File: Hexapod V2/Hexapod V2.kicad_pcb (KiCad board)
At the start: 4 copper layers, 140 x 90 mm, 43 parts, among them J1 Battery, U1 MPU6050, U2 NRF24L01_Breakout, U3 ACS712xLCTR-05B

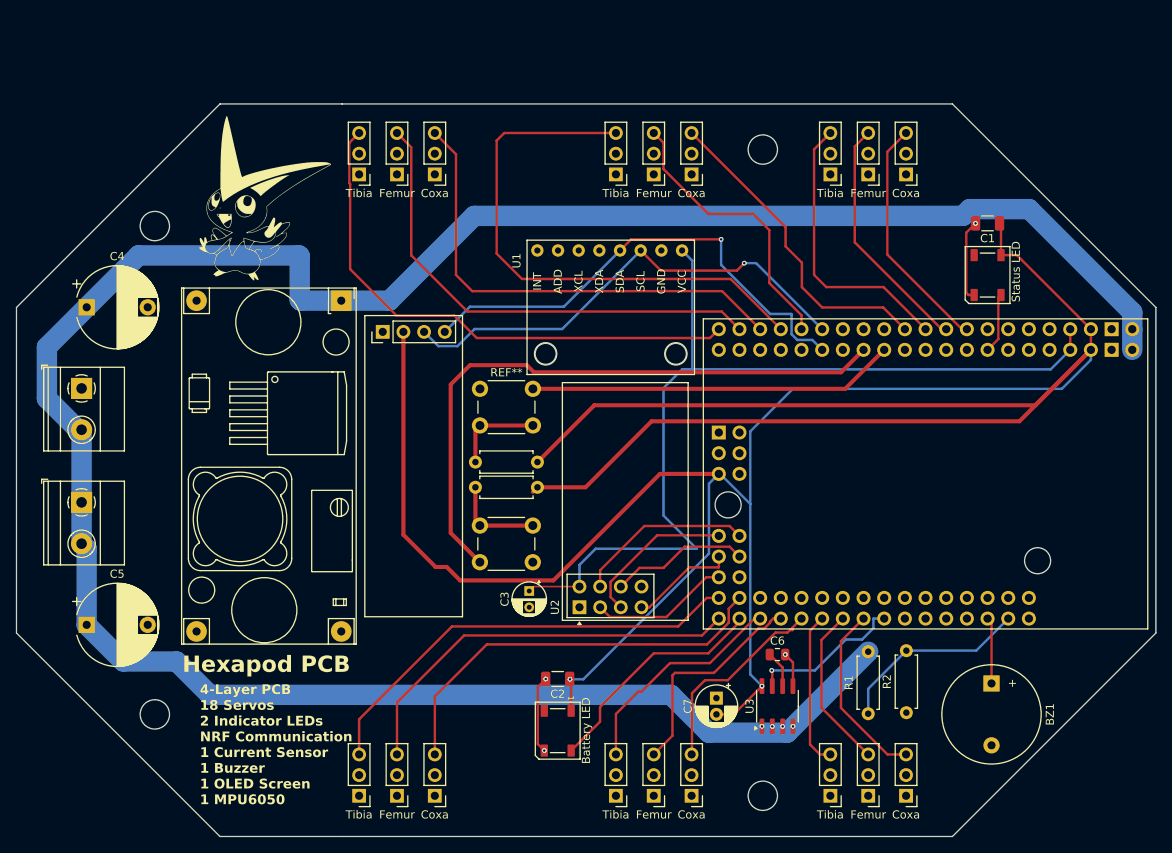
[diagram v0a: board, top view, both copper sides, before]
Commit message: Added Teensy
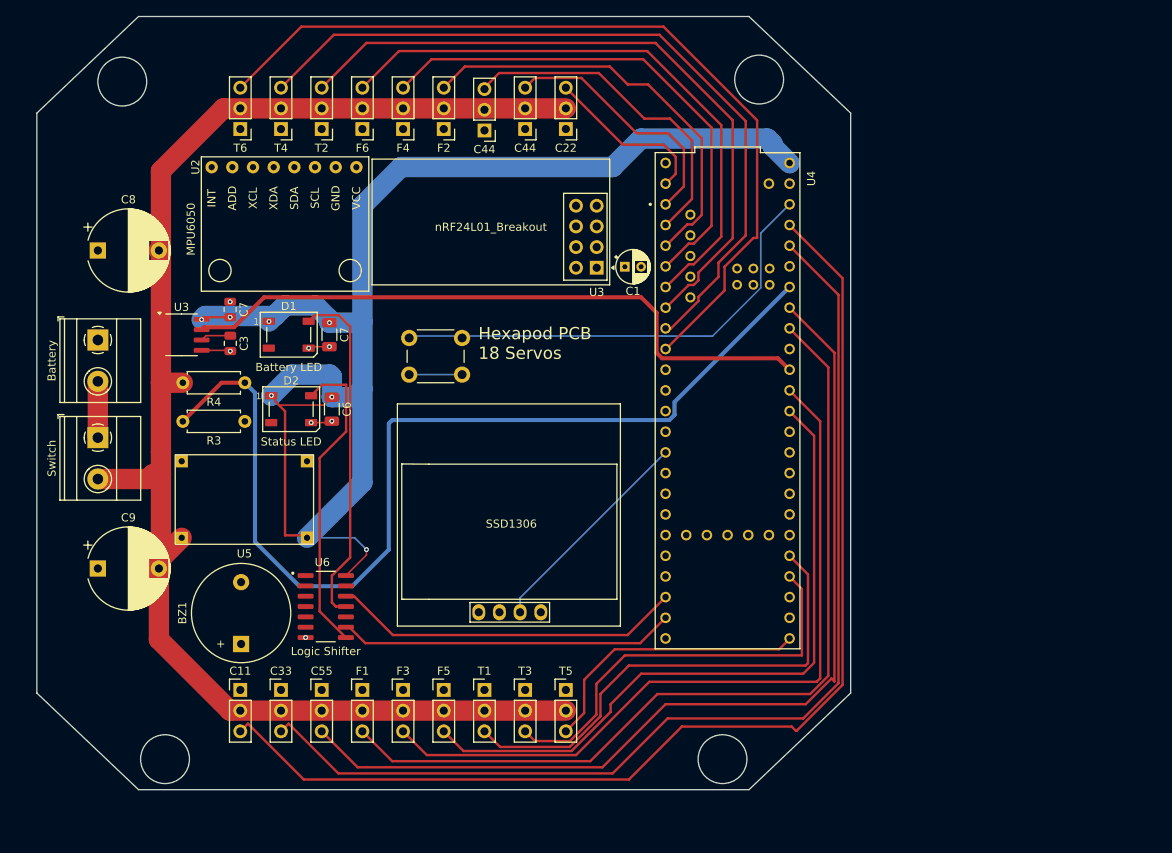
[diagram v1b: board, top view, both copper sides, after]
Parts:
- removed A1: Aurduino Mega 2560 Pro, Arduino Library:Clone_Mega2560_Pro_Socket
- removed Battery LED: WS2812B, LED_SMD:LED_WS2812B_PLCC4_5.0x5.0mm_P3.2mm
- removed C2: 104 0.1μF, Capacitor_SMD:C_1206_3216Metric
- removed C4, C5: 16V 1mF, Capacitor_THT:CP_Radial_D10.0mm_P7.50mm
- removed the C7 at (156.0, 118.0)
- removed Coxa (x6), Femur (x6), Tibia (x6): Conn_01x03_Pin, Connector_PinHeader_2.54mm:PinHeader_1x03_P2.54mm_Vertical
- removed G***: LOGO, Graphics:VICTINI
- removed J1 (x2): Battery, TerminalBlock_Phoenix:TerminalBlock_Phoenix_MKDS-1,5-2-5.08_1x02_P5.08mm_Horizontal
- removed R1 (x3), R2: 100kΩ, Resistor_THT:R_Axial_DIN0207_L6.3mm_D2.5mm_P7.62mm_Horizontal
- removed the REF** at (127.0, 80.0)
- removed the REF** at (126.9, 96.8)
- removed the REF** at (109.9, 69.2)
- removed the REF** at (115.0, 73.0)
- removed Status LED: WS2812B, LED_SMD:LED_WS2812B_PLCC4_5.0x5.0mm_P3.2mm
- removed U1: MPU6050, usini_sensors:module_mpu6050
- removed the U3 at (163.5, 119.0)
- added C11: Conn_01x03_Pin, Connector_PinHeader_2.54mm:PinHeader_1x03_P2.54mm_Vertical, F.Cu at (97.5, 117.0)
- added C22: Conn_01x03_Pin, Connector_PinHeader_2.54mm:PinHeader_1x03_P2.54mm_Vertical, F.Cu at (137.5, 48.1)
- added C33: Conn_01x03_Pin, Connector_PinHeader_2.54mm:PinHeader_1x03_P2.54mm_Vertical, F.Cu at (102.5, 117.0)
- added C44: Conn_01x03_Pin, Connector_PinHeader_2.54mm:PinHeader_1x03_P2.54mm_Vertical, F.Cu at (132.5, 48.1)
- added C44: Conn_01x03_Pin, Connector_PinHeader_2.54mm:PinHeader_1x03_P2.54mm_Vertical, F.Cu at (127.5, 48.2)
- added C55: Conn_01x03_Pin, Connector_PinHeader_2.54mm:PinHeader_1x03_P2.54mm_Vertical, F.Cu at (107.5, 117.0)
- added C7: 102 1nf, Capacitor_SMD:C_0805_2012Metric, F.Cu at (96.2, 70.2)
- added C7: 104 0.1μF, Capacitor_SMD:C_1206_3216Metric, F.Cu at (108.5, 73.3)
- added C8: 16V 1mF, Capacitor_THT:CP_Radial_D10.0mm_P7.50mm, F.Cu at (80.0, 63.0)
- added C9: 16V 1mF, Capacitor_THT:CP_Radial_D10.0mm_P7.50mm, F.Cu at (80.0, 102.1)
- added D1: Battery LED, LED_SMD:LED_WS2812B_PLCC4_5.0x5.0mm_P3.2mm, F.Cu at (103.5, 73.3)
- added D2: Status LED, LED_SMD:LED_WS2812B_PLCC4_5.0x5.0mm_P3.2mm, F.Cu at (103.8, 82.5)
- added F1: Conn_01x03_Pin, Connector_PinHeader_2.54mm:PinHeader_1x03_P2.54mm_Vertical, F.Cu at (112.5, 117.0)
- added F2: Conn_01x03_Pin, Connector_PinHeader_2.54mm:PinHeader_1x03_P2.54mm_Vertical, F.Cu at (122.5, 48.1)
- added F3: Conn_01x03_Pin, Connector_PinHeader_2.54mm:PinHeader_1x03_P2.54mm_Vertical, F.Cu at (117.5, 117.0)
- added F4: Conn_01x03_Pin, Connector_PinHeader_2.54mm:PinHeader_1x03_P2.54mm_Vertical, F.Cu at (117.5, 48.1)
- added F5: Conn_01x03_Pin, Connector_PinHeader_2.54mm:PinHeader_1x03_P2.54mm_Vertical, F.Cu at (122.5, 117.0)
- added F6: Conn_01x03_Pin, Connector_PinHeader_2.54mm:PinHeader_1x03_P2.54mm_Vertical, F.Cu at (112.5, 48.1)
- added J2: Battery, TerminalBlock_Phoenix:TerminalBlock_Phoenix_MKDS-1,5-2-5.08_1x02_P5.08mm_Horizontal, F.Cu at (80.0, 74.0)
- added J3: Switch, TerminalBlock_Phoenix:TerminalBlock_Phoenix_MKDS-1,5-2-5.08_1x02_P5.08mm_Horizontal, F.Cu at (80.0, 86.0)
- added R3: 100kΩ, Resistor_THT:R_Axial_DIN0207_L6.3mm_D2.5mm_P7.62mm_Horizontal, F.Cu at (98.1, 84.0)
- added R4: 100kΩ, Resistor_THT:R_Axial_DIN0207_L6.3mm_D2.5mm_P7.62mm_Horizontal, F.Cu at (98.1, 79.2)
- added REF**: SW_PUSH_6mm_H8mm, Button_Switch_THT:SW_PUSH_6mm_H8mm, F.Cu at (118.2, 73.8)
- added SSD1306: 128x64OLED, usini_sensors:128x64OLED, F.Cu at (130.8, 96.8)
- added T1: Conn_01x03_Pin, Connector_PinHeader_2.54mm:PinHeader_1x03_P2.54mm_Vertical, F.Cu at (127.5, 117.0)
- added T2: Conn_01x03_Pin, Connector_PinHeader_2.54mm:PinHeader_1x03_P2.54mm_Vertical, F.Cu at (107.5, 48.1)
- added T3: Conn_01x03_Pin, Connector_PinHeader_2.54mm:PinHeader_1x03_P2.54mm_Vertical, F.Cu at (132.5, 117.0)
- added T4: Conn_01x03_Pin, Connector_PinHeader_2.54mm:PinHeader_1x03_P2.54mm_Vertical, F.Cu at (102.5, 48.1)
- added T5: Conn_01x03_Pin, Connector_PinHeader_2.54mm:PinHeader_1x03_P2.54mm_Vertical, F.Cu at (137.5, 117.0)
- added T6: Conn_01x03_Pin, Connector_PinHeader_2.54mm:PinHeader_1x03_P2.54mm_Vertical, F.Cu at (97.5, 48.1)
- added U3: ACS712xLCTR-05B, Package_SO:SOIC-8_3.9x4.9mm_P1.27mm, F.Cu at (90.3, 73.4)
- added U3: nRF24L01_Breakout, teensy:nRF24L01_Breakout, F.Cu at (141.3, 65.1)
- added U4: Teensy 4.1, usini_sensors:MODULE_DEV-16771, F.Cu at (157.4, 81.5)
- added U5: Buck, Arduino Library:Buck, F.Cu at (98.0, 88.0)
- added U6: Logic Shifter, Logic Shifters:SOIC127P600X175-14N, F.Cu at (108.0, 106.8)
- C1: value 104 0.1μF -> 16V 22μF; footprint Capacitor_SMD:C_1206_3216Metric -> Capacitor_THT:CP_Radial_D4.0mm_P2.00mm
- C3: value 16V 22μF -> 102 1nf; footprint Capacitor_THT:CP_Radial_D4.0mm_P2.00mm -> Capacitor_SMD:C_0805_2012Metric
- C6: value 102 1nf -> 104 0.1μF; footprint Capacitor_SMD:C_0805_2012Metric -> Capacitor_SMD:C_1206_3216Metric
- U2: value NRF24L01_Breakout -> MPU6050; footprint RF_Module:nRF24L01_Breakout -> usini_sensors:module_mpu6050
- moved BZ1 92.3 mm to (97.6, 111.3), turned to 90 degrees
- moved U2 70.5 mm to (94.0, 52.8), turned to -90 degrees
- moved C6 62.5 mm to (108.8, 82.5), turned to -90 degrees
- moved C3 47.7 mm to (96.3, 74.4)
- moved C1 44.9 mm to (144.8, 65.0), turned to 0 degrees
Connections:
- C1 pad 1: +5V -> +3.3V
- C3 pad 1: +3.3V -> Net-(U3-FILTER)
- C6 pad 1: Net-(U3-FILTER) -> +5V
- U2 pad 1: GND -> +3.3V
- U2 pad 2: +3.3V -> GND
- U2 pad 3: CE -> SCL
- U2 pad 4: CSN -> SDA
- U2 pad 5: SCK -> unconnected-(U2-XDA-Pad5)
- U2 pad 6: MOSI -> unconnected-(U2-XCL-Pad6)
- U2 pad 7: MISO -> unconnected-(U2-ADD-Pad7)
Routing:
- net +5V: track 394.5 -> 184.8 mm, vias 2 -> 7
- net VIN: track 300.0 -> 187.2 mm, vias 4 -> 0
- net VD Reading: track 23.8 -> 122.8 mm
- net LED1: track 7.42 -> 85.9 mm
- net unconnected-(A1-D16/TX2-PadD16): track 76.5 -> 0.00 mm
- net S18: track 66.5 -> 141.6 mm
- net S17: track 59.8 -> 132.2 mm
- net Buzzer: track 8.17 -> 70.1 mm
- net +3.3V: track 116.5 -> 178.5 mm
- net Current Reading: track 19.1 -> 80.5 mm, vias 1 -> 0
- net S16: track 58.6 -> 117.7 mm
- net S14: track 34.8 -> 93.3 mm
- net LED2: track 28.7 -> 80.0 mm
- net S9: track 54.7 -> 104.4 mm
- net S6: track 27.5 -> 72.9 mm
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- removed copper zone on In2.Cu, net S+
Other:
- board size 140 x 90 mm -> 100 x 95 mm
- board text added: "Hexapod PCB 18 Servos"
- board text removed: "4-Layer PCB 18 Servos 2 Indicator LEDs NRF Communication 1 Current Sensor 1 Buzzer 1 OLED Screen 1 MPU6050"
- board text removed: "Hexapod PCB"
